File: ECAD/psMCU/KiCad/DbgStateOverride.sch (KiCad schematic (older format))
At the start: 4 parts, among them U433 74HC594PW, U434 74HC157PW

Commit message: Sch: Cleanup + Small fixes
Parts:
- added C503: 0u1, NoRef_Footprints:C_0603_1608Metric_NoRef, symbol Device:C_Small
- added U459: 74HC157PW, Package_SO:TSSOP-16_4.4x5mm_P0.65mm, symbol 74xx:74LS157
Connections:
- net +5V: now also C503.2, U459.16 (VCC)
- net GND: now also C503.1, U459.10 (I1c), U459.13 (I1d), U459.15 (E), U459.6 (I1b), U459.8 (GND)
- net at U433.15 (Q0), U434.3 (I1a): now also U459.1 (S)
- net at U433.5 (Q5): now also U459.3 (I1a)
- new net C_Step_I: U459.5 (I0b)
- new net C_Step_O: U459.7 (Zb)
- new net Dec_Clk_F_I: U459.14 (I0d)
- new net Dec_Clk_F_O: U459.12 (Zd)
- new net Inc_Clk_F_I: U459.11 (I0c)
- new net Inc_Clk_F_O: U459.9 (Zc)
- new net Reset_I: U459.2 (I0a)
- new net Reset_O: U459.4 (Za)
- no-connect marks 4 -> 3
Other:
- moved on the sheet: C475, C476, U433, U434

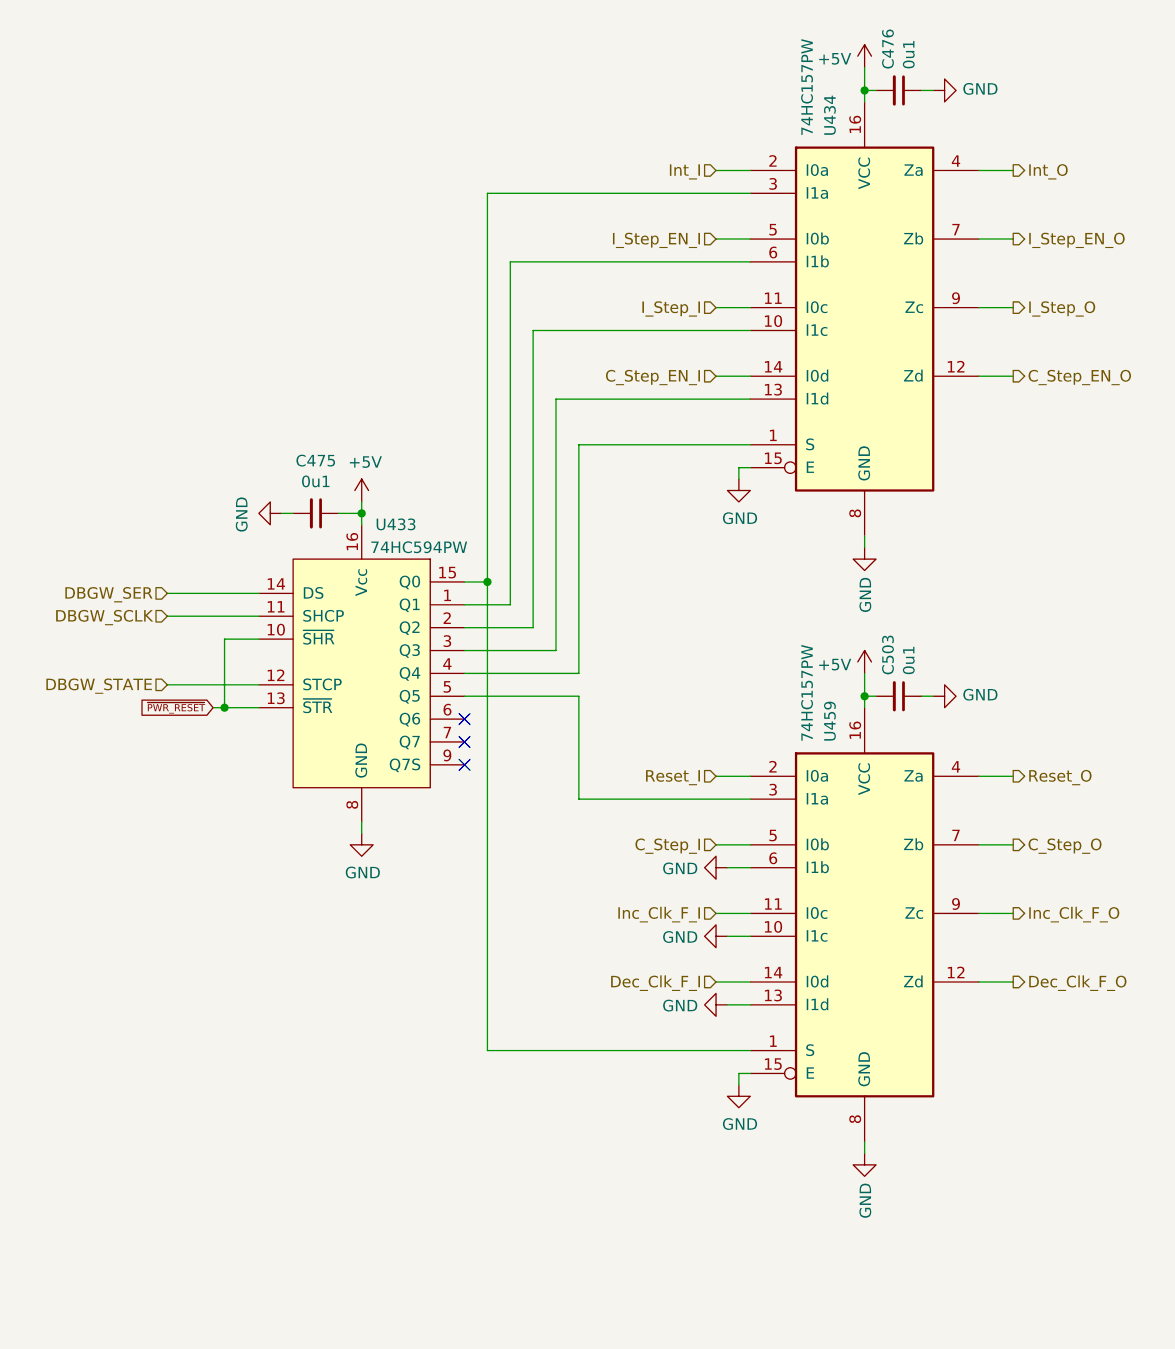
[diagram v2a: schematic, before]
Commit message: Sch: More cleanup, fixed page descriptions.
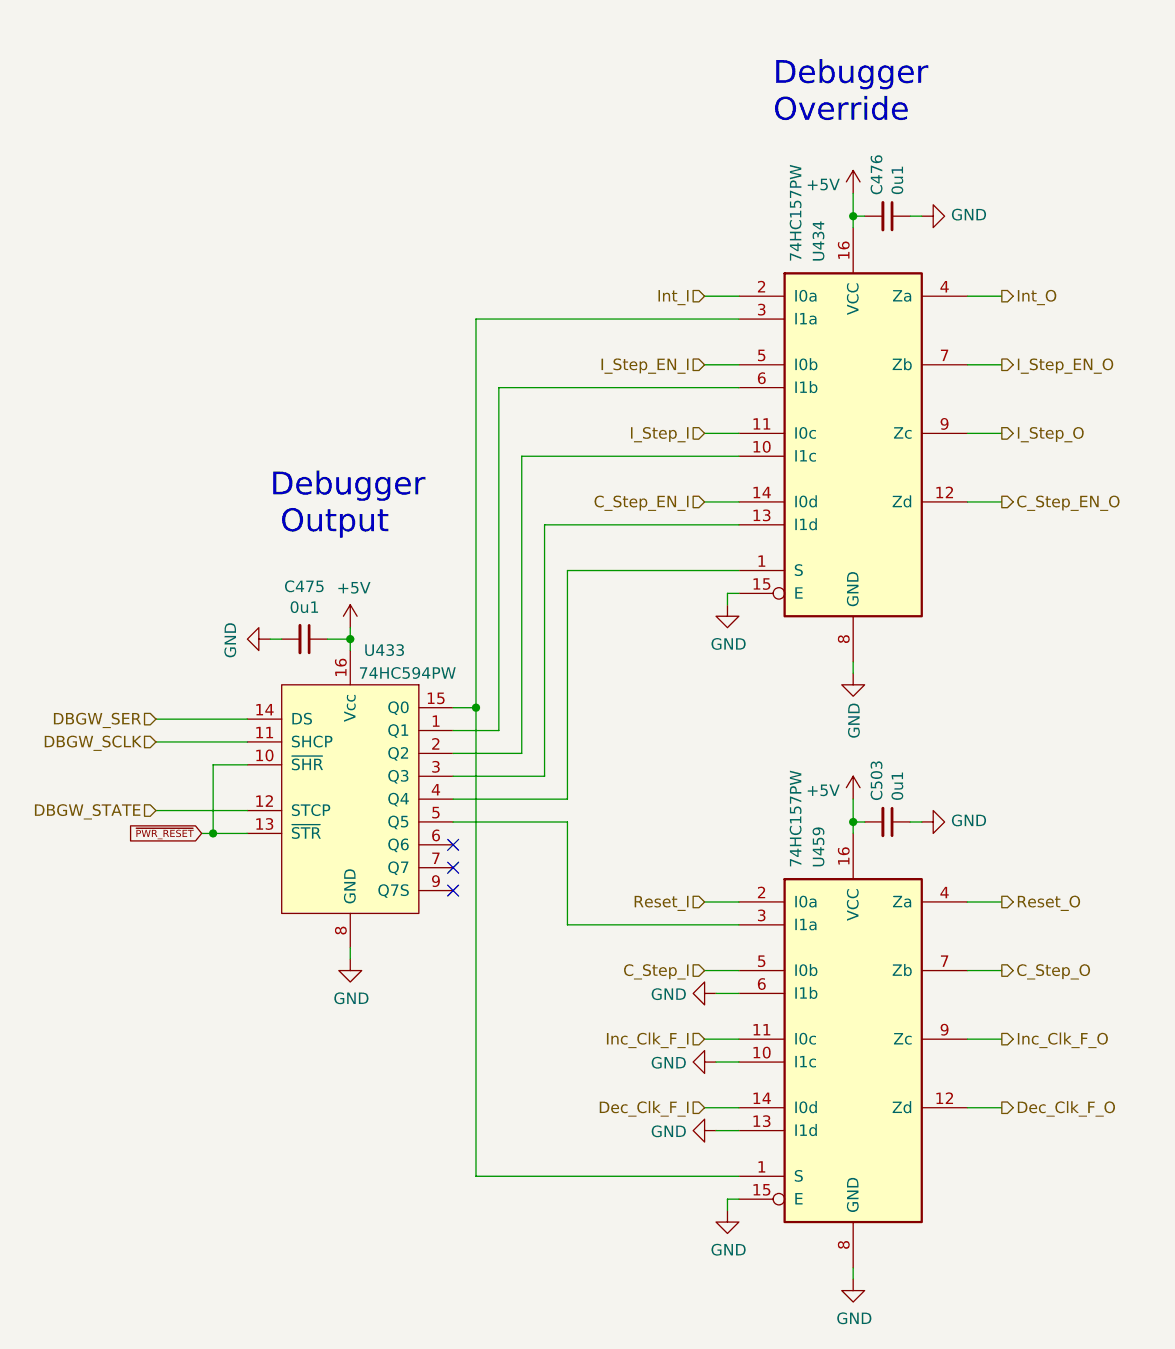
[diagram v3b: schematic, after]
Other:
- note added: "Debugger\n Output"
- note added: "Debugger\nOverride"
- moved on the sheet: C475, C476, C503, U433, U434, U459
